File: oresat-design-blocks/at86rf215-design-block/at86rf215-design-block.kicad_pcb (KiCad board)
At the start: 4 copper layers, 61.3 x 44.1 mm, 80 parts, among them J1 SMA, J10 Conn_01x08, J11 Conn_01x05, J12 Conn_01x08, J2 USB4105-GF-A, J3 Conn_01x06, J4 SMA, J6 Conn_01x06, J7 SMA, J8 SMA, J9 Screw_Terminal_01x02, SW1 RESET, U1 AT86RF215, U2 LP2985AIM5-1.8_NOPB, U3 2450FB15A050E, U4 NCS2-62+, U5 QPC1022, X1 TXETALSANF-26.000000

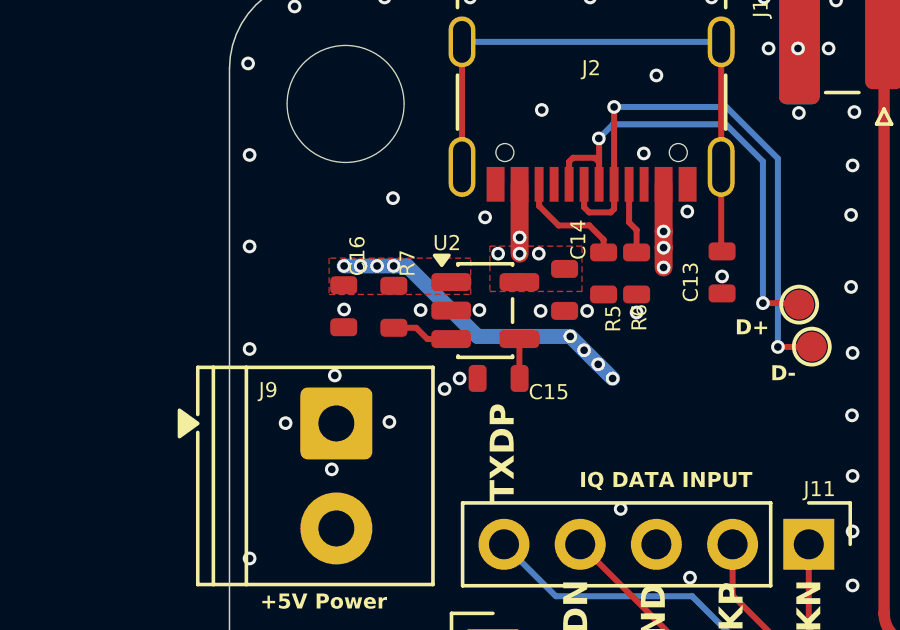
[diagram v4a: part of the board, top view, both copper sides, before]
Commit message: fixed USBC power LDO vin vout swap
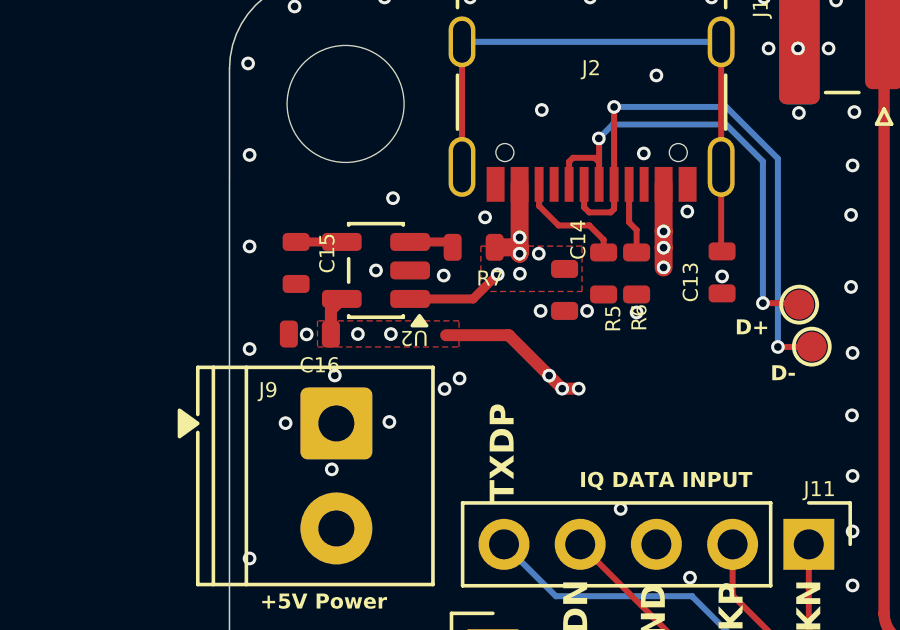
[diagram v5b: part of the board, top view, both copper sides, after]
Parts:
- moved C15 7.77 mm to (93.0, 63.8), turned to -90 degrees
- moved U2 3.88 mm to (95.7, 64.0), turned to 180 degrees
- moved R7 3.32 mm to (99.0, 63.3), turned to 180 degrees
- moved C16 1.46 mm to (93.5, 66.2), turned to 180 degrees
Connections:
- R7 pad 1: +3.3V -> +5V
- U2 pad 1: +3.3V -> +5V
- U2 pad 5: +5V -> +3.3V
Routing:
- net +5V: track 101.1 -> 106.1 mm, vias 9 -> 10
- net +3.3V: track 23.6 -> 19.6 mm, vias 18 -> 15
- net Net-(U2-EN): track 2.07 -> 1.49 mm
